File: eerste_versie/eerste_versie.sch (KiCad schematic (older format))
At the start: 17 parts, among them J1 105017-1001, U1 ESP32-WROOM-32U, U2 AMS1117-3.3

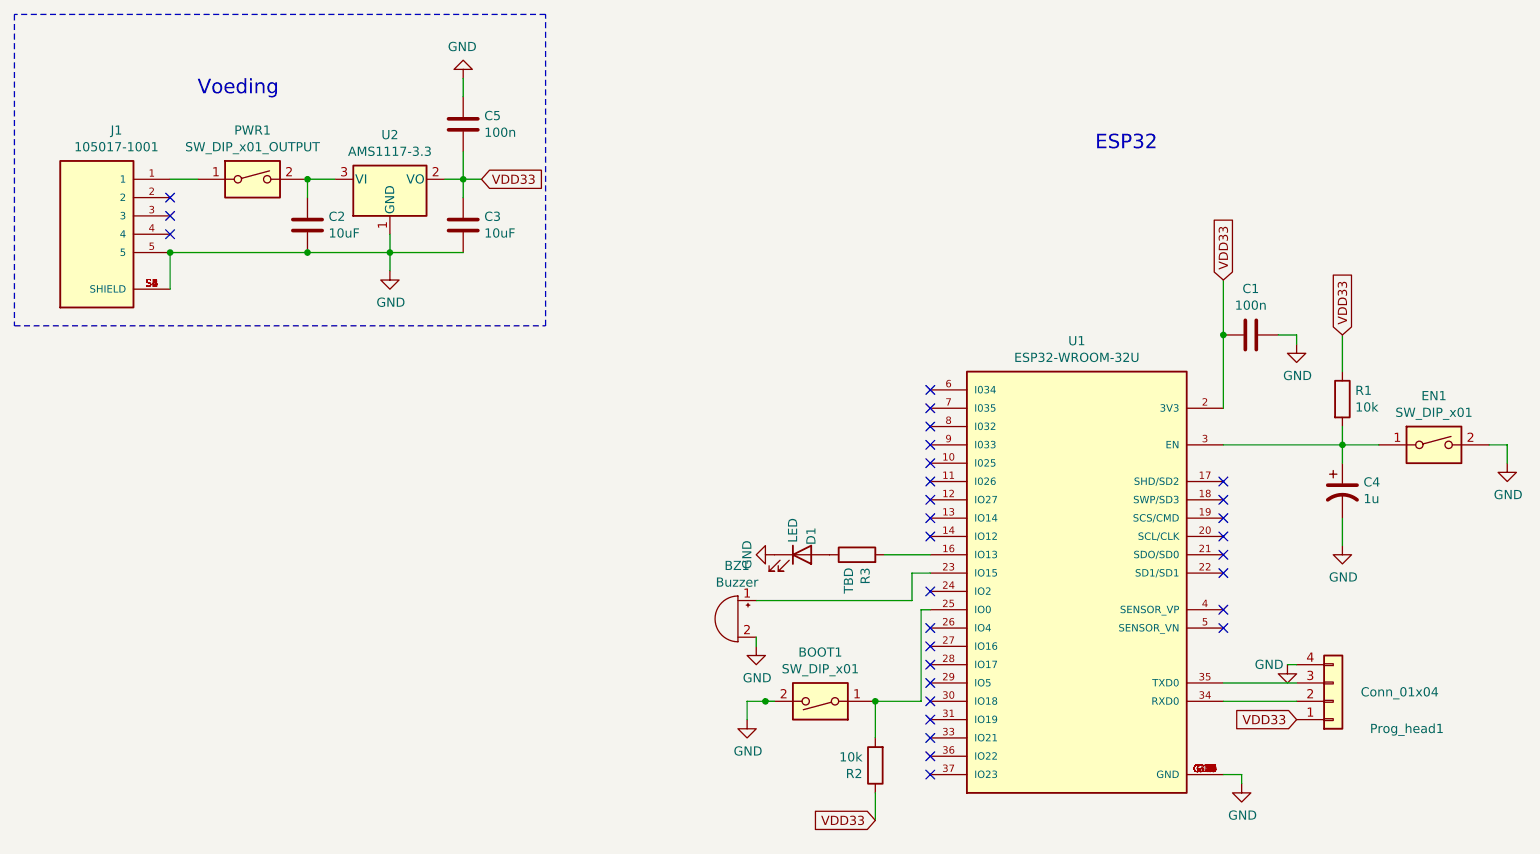
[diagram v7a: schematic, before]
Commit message: batterij toevoeging
- printkroonsteentje voor aansluiting van batterijkabels toegevoegd
- pull-up weerstand aan IO5 toegevoegd
-3D modellen toegevoegd
- silkscreens in orde gebracht
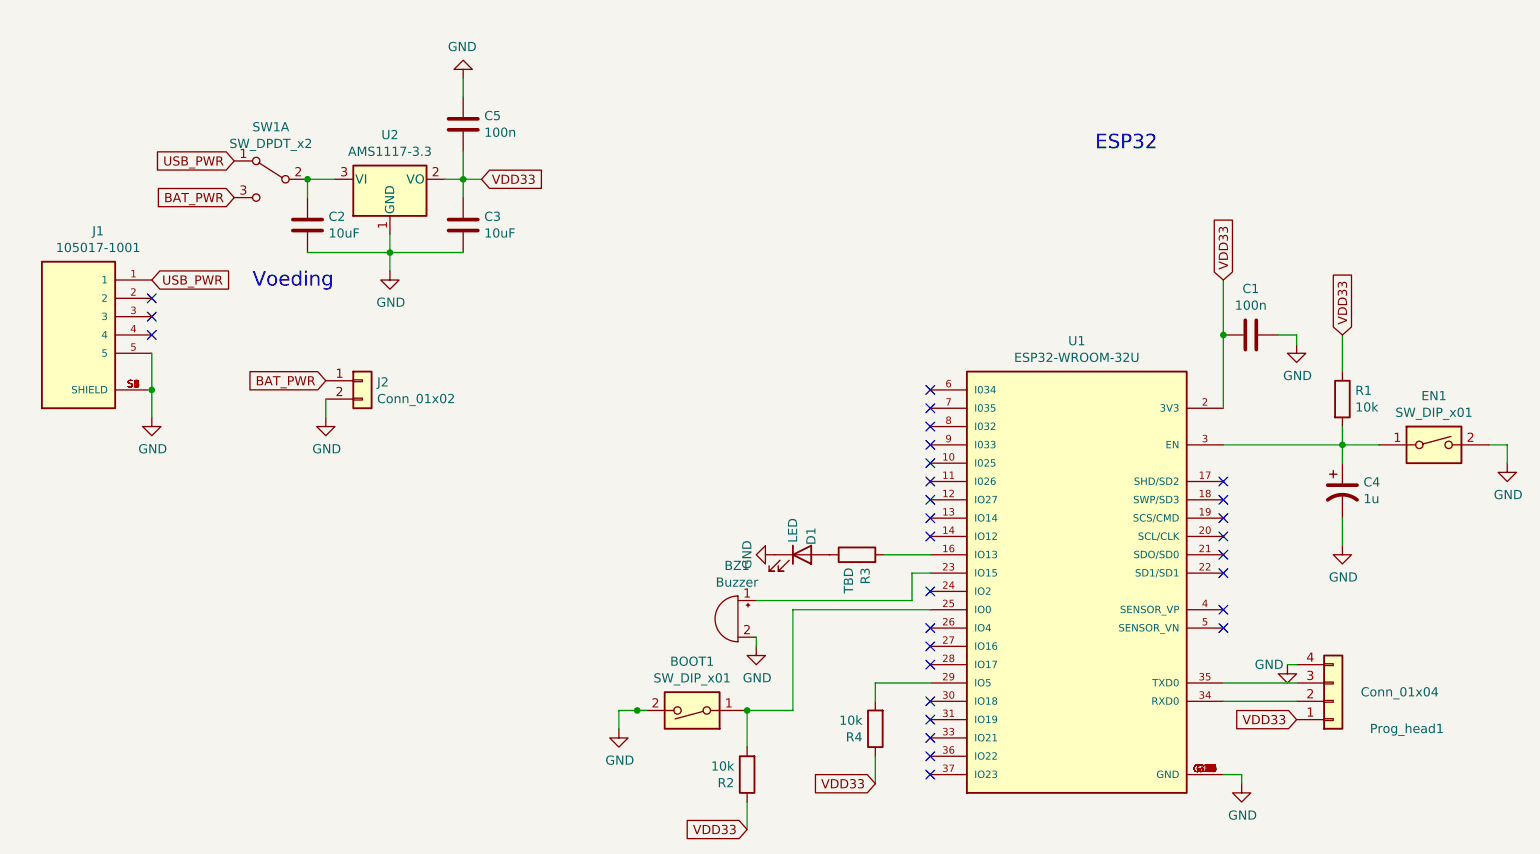
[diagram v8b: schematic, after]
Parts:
- removed PWR1: SW_DIP_x01_OUTPUT, sparkfun:SWITCH_SPST_SMD_A, symbol eerste_versie-rescue:SW_DIP_x01_OUTPUT-Switch_out
- added J2: Conn_01x02, TerminalBlock_Phoenix:TerminalBlock_Phoenix_MKDS-1,5-2-5.08_1x02_P5.08mm_Horizontal, symbol Connector_Generic:Conn_01x02
- added R4: 10k, Resistor_SMD:R_0805_2012Metric_Pad1.20x1.40mm_HandSolder, symbol Device:R
- added SW1: SW_DPDT_x2, sparkfun:SWITCH_SPST_SMD_A, symbol Switch_3_out:SW_DPDT_x2
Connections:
- net GND: now also J2.2 (Pin_2)
- net VDD33: now also R4.1
- net at U1.29 (IO5): now also R4.2
- net at C2.1, U2.3 (VI): now also SW1.2 (B)
- net USB_PWR: now reaches J1.1
- net USB_PWR: now also SW1.1 (A)
- new net BAT_PWR: J2.1 (Pin_1), SW1.3 (C)
- no-connect marks 30 -> 29
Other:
- moved on the sheet: BOOT1, J1, R2
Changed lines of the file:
@@
 	1    0    0    -1
 $EndComp
-Wire Wire Line
-	1300 1350 1450 1350
-$Comp
-L eerste_versie-rescue:SW_DIP_x01_OUTPUT-Switch_out PWR1
-U 1 1 6044F04F
-P 1750 1350
-F 0 "PWR1" H 1750 1617 50  0000 C CNN
-F 1 "SW_DIP_x01_OUTPUT" H 1750 1526 50  0000 C CNN
-F 2 "sparkfun:SWITCH_SPST_SMD_A" H 1750 1350 50  0001 C CNN
-F 3 "~" H 1750 1350 50  0001 C CNN
-	1    1750 1350
-	1    0    0    -1
-$EndComp
-Connection ~ 2050 1350
-Text Notes 1450 900  0    79   ~ 0
+Text Notes 1750 1950 0    79   ~ 0
 Voeding
 Text GLabel 3000 1350 2    50   Input ~ 0
 VDD33
-$Comp
-L 105017-1001:105017-1001 J1
-U 1 1 6058A93D
-P 900 1650
-F 0 "J1" H 1007 2217 50  0000 C CNN
-F 1 "105017-1001" H 1007 2126 50  0000 C CNN
-F 2 "105017-1001:MOLEX_105017-1001" H 900 1650 50  0001 L BNN
-F 3 "" H 900 1650 50  0001 L BNN
-F 4 "MOLEX" H 900 1650 50  0001 L BNN "MANUFACTURER"
-F 5 "2.9mm" H 900 1650 50  0001 L BNN "MAXIMUM_PACKAGE_HIEGHT"
-F 6 "Manufacturer Recommendations" H 900 1650 50  0001 L BNN "STANDARD"
-F 7 "F" H 900 1650 50  0001 L BNN "PARTREV"
-	1    900  1650
-	1    0    0    -1
-$EndComp
-Wire Wire Line
-	1300 1750 1300 1950
-Wire Wire Line
-	1300 1750 2050 1750
-Connection ~ 1300 1750
-Connection ~ 2050 1750
 Wire Wire Line
 	2050 1750 2500 1750
-NoConn ~ 1300 1450
-NoConn ~ 1300 1550
-NoConn ~ 1300 1650
-Wire Notes Line
-	450  450  450  2150
+NoConn ~ 1200 2000
+NoConn ~ 1200 2100
+NoConn ~ 1200 2200
 Text Notes 6350 1200 0    79   ~ 0
 ESP32
@@
 	1    0    0    -1
 $EndComp
-Wire Wire Line
-	5400 3700 5400 4200
-Wire Wire Line
-	5450 3700 5400 3700
 $Comp
 L power:GND #PWR09
@@
 	0    -1   -1   0
 $EndComp
-Connection ~ 4550 4200
-Wire Wire Line
-	4600 4200 4550 4200
+Connection ~ 3850 4250
+Wire Wire Line
+	3900 4250 3850 4250
 $Comp
 L Device:Buzzer BZ1
@@
 L Switch:SW_DIP_x01 BOOT1
 U 1 1 60452495
-P 4850 4200
-F 0 "BOOT1" H 4850 3933 50  0000 C CNN
-F 1 "SW_DIP_x01" H 4850 4024 50  0000 C CNN
-F 2 "434111043826:434111043826" H 4850 4200 50  0001 C CNN
-F 3 "~" H 4850 4200 50  0001 C CNN
-	1    4850 4200
+P 4150 4250
+F 0 "BOOT1" H 4150 3983 50  0000 C CNN
+F 1 "SW_DIP_x01" H 4150 4074 50  0000 C CNN
+F 2 "434111043826:434111043826" H 4150 4250 50  0001 C CNN
+F 3 "~" H 4150 4250 50  0001 C CNN
+	1    4150 4250
 	-1   0    0    1
 $EndComp
-Connection ~ 5150 4200
-Wire Wire Line
-	5150 4200 5400 4200
-Wire Wire Line
-	5150 4850 5150 4700
-Text GLabel 5150 4850 0    50   Input ~ 0
-VDD33
-Wire Wire Line
-	5150 4400 5150 4200
+Connection ~ 4450 4250
+Wire Wire Line
+	4450 4250 4700 4250
+Wire Wire Line
+	4450 4900 4450 4750
+Text GLabel 4450 4900 0    50   Input ~ 0
+VDD33
+Wire Wire Line
+	4450 4450 4450 4250
 $Comp
 L Device:R R2
 U 1 1 60511A7D
-P 5150 4550
-F 0 "R2" H 5220 4596 50  0000 L CNN
-F 1 "10k" H 5220 4505 50  0000 L CNN
-F 2 "Resistor_SMD:R_0805_2012Metric_Pad1.20x1.40mm_HandSolder" V 5080 4550 50  0001 C CNN
-F 3 "~" H 5150 4550 50  0001 C CNN
-	1    5150 4550
+P 4450 4600
+F 0 "R2" H 4520 4646 50  0000 L CNN
+F 1 "10k" H 4520 4555 50  0000 L CNN
+F 2 "Resistor_SMD:R_0805_2012Metric_Pad1.20x1.40mm_HandSolder" V 4380 4600 50  0001 C CNN
+F 3 "~" H 4450 4600 50  0001 C CNN
+	1    4450 4600
 	-1   0    0    1
 $EndComp
@@
 L power:GND #PWR04
 U 1 1 60453368
-P 4450 4300
-F 0 "#PWR04" H 4450 4050 50  0001 C CNN
-F 1 "GND" H 4455 4127 50  0000 C CNN
-F 2 "" H 4450 4300 50  0001 C CNN
-F 3 "" H 4450 4300 50  0001 C CNN
-	1    4450 4300
-	1    0    0    -1
-$EndComp
-Wire Wire Line
-	4550 4200 4450 4200
-Wire Wire Line
-	4450 4200 4450 4300
+P 3750 4350
+F 0 "#PWR04" H 3750 4100 50  0001 C CNN
+F 1 "GND" H 3755 4177 50  0000 C CNN
+F 2 "" H 3750 4350 50  0001 C CNN
+F 3 "" H 3750 4350 50  0001 C CNN
+	1    3750 4350
+	1    0    0    -1
+$EndComp
+Wire Wire Line
+	3850 4250 3750 4250
+Wire Wire Line
+	3750 4250 3750 4350
 NoConn ~ 5450 2900
 NoConn ~ 5450 3000
@@
 NoConn ~ 5450 3900
 NoConn ~ 5450 4000
-NoConn ~ 5450 4100
 NoConn ~ 5450 4200
 NoConn ~ 5450 4300
@@
 Wire Wire Line
 	7700 2800 7700 2900
-Wire Notes Line
-	3350 2150 3350 450
-Wire Notes Line
-	3350 450  450  450
-Wire Notes Line
-	450  2150 3350 2150
 NoConn ~ 5450 3300
 Wire Wire Line
@@
 	1    0    0    1
 $EndComp
+$Comp
+L Connector_Generic:Conn_01x02 J2
+U 1 1 606E0DE4
+P 2350 2450
+F 0 "J2" H 2430 2442 50  0000 L CNN
+F 1 "Conn_01x02" H 2430 2351 50  0000 L CNN
+F 2 "TerminalBlock_Phoenix:TerminalBlock_Phoenix_MKDS-1,5-2-5.08_1x02_P5.08mm_Horizontal" H 2350 2450 50  0001 C CNN
+F 3 "~" H 2350 2450 50  0001 C CNN
+	1    2350 2450
+	1    0    0    -1
+$EndComp
+$Comp
+L power:GND #PWR011
+U 1 1 606F0CF9
+P 2150 2650
+F 0 "#PWR011" H 2150 2400 50  0001 C CNN
+F 1 "GND" H 2155 2477 50  0000 C CNN
+F 2 "" H 2150 2650 50  0001 C CNN
+F 3 "" H 2150 2650 50  0001 C CNN
+	1    2150 2650
+	1    0    0    -1
+$EndComp
+Wire Wire Line
+	2150 2550 2150 2650
+Text GLabel 1200 1900 2    50   Input ~ 0
+USB_PWR
+Text GLabel 1650 1250 0    50   Input ~ 0
+USB_PWR
+Text GLabel 2150 2450 0    50   Input ~ 0
+BAT_PWR
+Text GLabel 1650 1450 0    50   Input ~ 0
+BAT_PWR
+Connection ~ 1200 2500
+Wire Wire Line
+	1200 2500 1200 2650
+Wire Wire Line
+	1200 2300 1200 2500
+$Comp
+L power:GND #PWR010
+U 1 1 606EE915
+P 1200 2650
+F 0 "#PWR010" H 1200 2400 50  0001 C CNN
+F 1 "GND" H 1205 2477 50  0000 C CNN
+F 2 "" H 1200 2650 50  0001 C CNN
+F 3 "" H 1200 2650 50  0001 C CNN
+	1    1200 2650
+	1    0    0    -1
+$EndComp
+$Comp
+L 105017-1001:105017-1001 J1
+U 1 1 6058A93D
+P 800 2200
+F 0 "J1" H 907 2767 50  0000 C CNN
+F 1 "105017-1001" H 907 2676 50  0000 C CNN
+F 2 "105017-1001:MOLEX_105017-1001" H 800 2200 50  0001 L BNN
+F 3 "" H 800 2200 50  0001 L BNN
+F 4 "MOLEX" H 800 2200 50  0001 L BNN "MANUFACTURER"
+F 5 "2.9mm" H 800 2200 50  0001 L BNN "MAXIMUM_PACKAGE_HIEGHT"
+F 6 "Manufacturer Recommendations" H 800 2200 50  0001 L BNN "STANDARD"
+F 7 "F" H 800 2200 50  0001 L BNN "PARTREV"
+	1    800  2200
+	1    0    0    -1
+$EndComp
+Wire Wire Line
+	4700 4250 4700 3700
+Wire Wire Line
+	4700 3700 5450 3700
+$Comp
+L Device:R R4
+U 1 1 606FFD84
+P 5150 4350
+F 0 "R4" H 5220 4396 50  0000 L CNN
+F 1 "10k" H 5220 4305 50  0000 L CNN
+F 2 "Resistor_SMD:R_0805_2012Metric_Pad1.20x1.40mm_HandSolder" V 5080 4350 50  0001 C CNN
+F 3 "~" H 5150 4350 50  0001 C CNN
+	1    5150 4350
+	-1   0    0    1
+$EndComp
+Wire Wire Line
+	5450 4100 5150 4100
+Wire Wire Line
+	5150 4100 5150 4200
+Text GLabel 5150 4650 0    50   Input ~ 0
+VDD33
+Wire Wire Line
+	5150 4650 5150 4500
+$Comp
+L Switch_3_out:SW_DPDT_x2 SW1
+U 1 1 60708053
+P 1850 1350
+F 0 "SW1" H 1850 1635 50  0000 C CNN
+F 1 "SW_DPDT_x2" H 1850 1544 50  0000 C CNN
+F 2 "sparkfun:SWITCH_SPST_SMD_A" H 1850 1350 50  0001 C CNN
+F 3 "~" H 1850 1350 50  0001 C CNN
+	1    1850 1350
+	-1   0    0    -1
+$EndComp
+Connection ~ 2050 1350
 $EndSCHEMATC
